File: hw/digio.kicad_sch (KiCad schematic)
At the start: 11 parts, among them U17 SN74LVC2T45DCUR

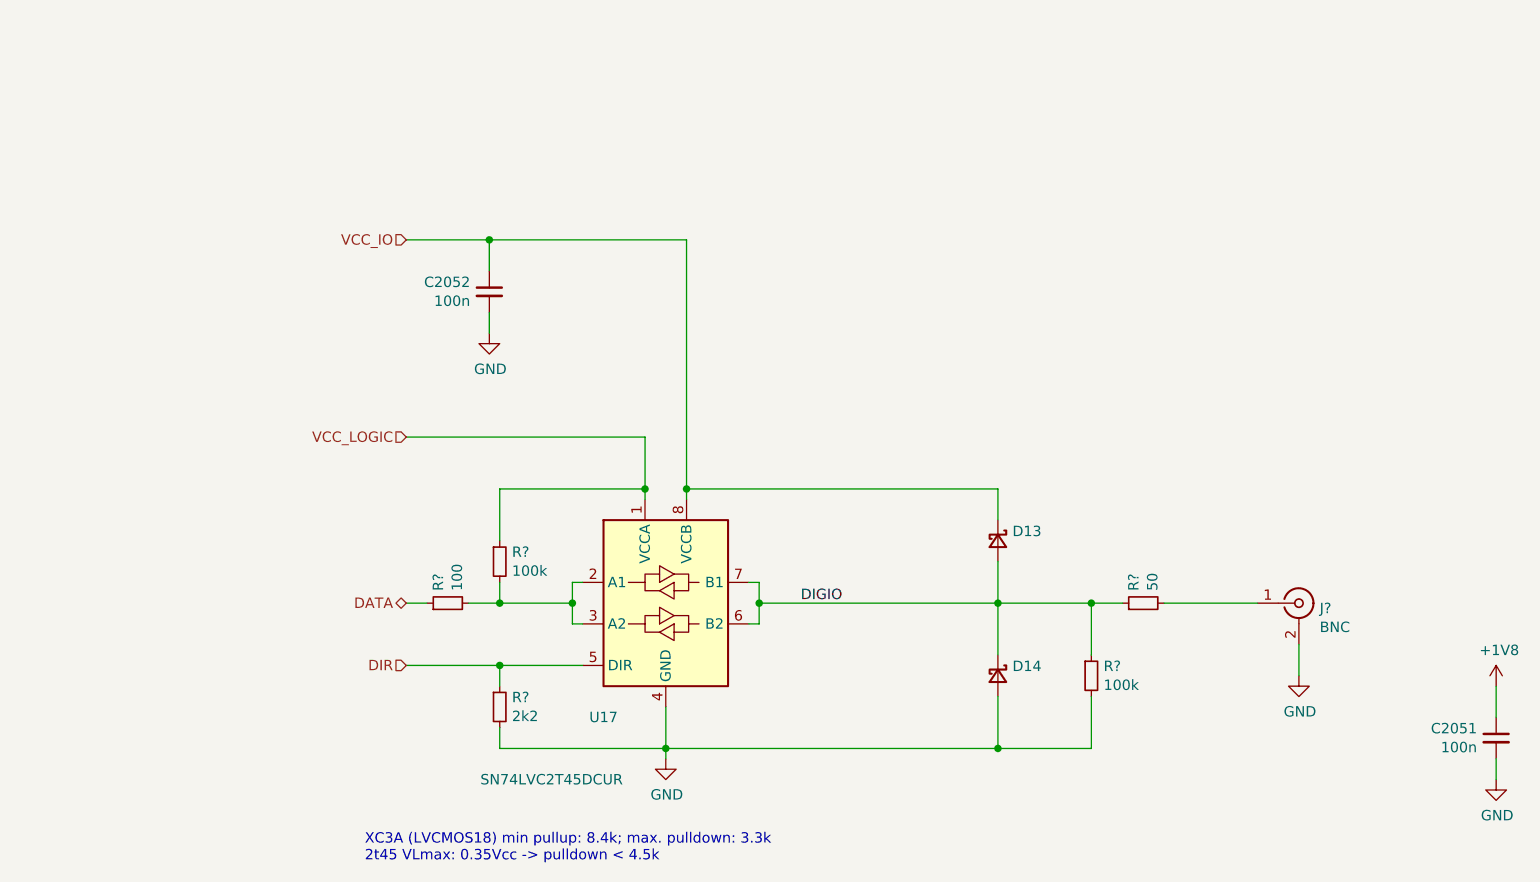
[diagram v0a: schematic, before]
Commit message: basic schematic, started layout (placing first components)
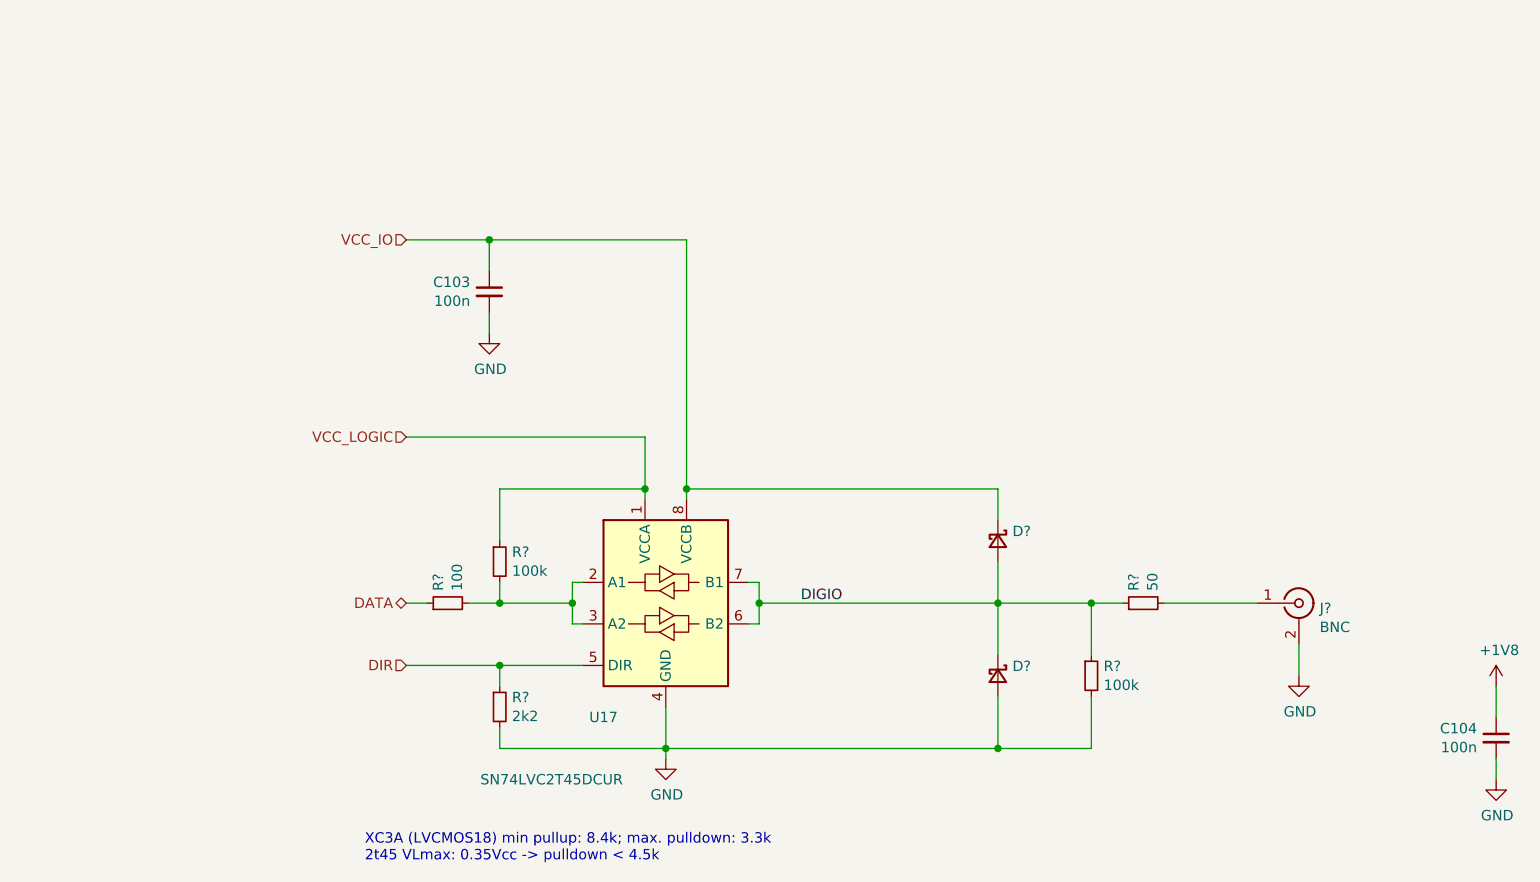
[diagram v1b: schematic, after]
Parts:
- renumbered C2052 to C103, C2051 to C104, D14 to D?, D13 to D?
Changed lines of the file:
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@@
     (effects (font (size 1.27 1.27)) (justify left bottom))
   )
-  (label "DIGIO" (at 152.4 105.41 0)
+  (label "DIGIO" (at 152.4 105.41 0) (fields_autoplaced)
     (effects (font (size 1.27 1.27)) (justify left bottom))
   )
-  (hierarchical_label "DATA" (shape bidirectional) (at 104.14 105.41 180)
+  (hierarchical_label "DATA" (shape bidirectional) (at 104.14 105.41 180) (fields_autoplaced)
     (effects (font (size 1.27 1.27)) (justify right))
   )
-  (hierarchical_label "VCC_LOGIC" (shape input) (at 104.14 85.09 180)
+  (hierarchical_label "VCC_LOGIC" (shape input) (at 104.14 85.09 180) (fields_autoplaced)
     (effects (font (size 1.27 1.27)) (justify right))
   )
-  (hierarchical_label "DIR" (shape input) (at 104.14 113.03 180)
+  (hierarchical_label "DIR" (shape input) (at 104.14 113.03 180) (fields_autoplaced)
     (effects (font (size 1.27 1.27)) (justify right))
   )
-  (hierarchical_label "VCC_IO" (shape input) (at 104.14 60.96 180)
+  (hierarchical_label "VCC_IO" (shape input) (at 104.14 60.96 180) (fields_autoplaced)
     (effects (font (size 1.27 1.27)) (justify right))
   )
@@
           (reference "J?") (unit 1)
         )
-        (path "/7c8a1f8d-8834-4c9b-aaae-1f231e9b09a1/00000000-0000-0000-0000-0000612b1274/00000000-0000-0000-0000-0000611e90a8"
-          (reference "J?") (unit 1)
-        )
         (path "/7c8a1f8d-8834-4c9b-aaae-1f231e9b09a1/00000000-0000-0000-0000-000060aabc24/00000000-0000-0000-0000-000060f79994"
           (reference "J10") (unit 1)
-        )
-        (path "/7c8a1f8d-8834-4c9b-aaae-1f231e9b09a1/00000000-0000-0000-0000-0000612b1274/00000000-0000-0000-0000-0000611783bc"
-          (reference "J?") (unit 1)
         )
         (path "/7c8a1f8d-8834-4c9b-aaae-1f231e9b09a1/00000000-0000-0000-0000-000060b16d71"
@@
   (symbol (lib_id "Device:C_Small") (at 237.49 121.92 0) (mirror y) (unit 1)
     (in_bom yes) (on_board yes) (dnp no)
-    (property "Reference" "C2051" (at 235.1532 120.7516 0)
+    (property "Reference" "C104" (at 235.1532 120.7516 0)
       (effects (font (size 1.27 1.27)) (justify left))
     )
@@
   (symbol (lib_id "Device:C_Small") (at 114.3 67.31 0) (mirror y) (unit 1)
     (in_bom yes) (on_board yes) (dnp no)
-    (property "Reference" "C2052" (at 111.9632 66.1416 0)
+    (property "Reference" "C103" (at 111.9632 66.1416 0)
       (effects (font (size 1.27 1.27)) (justify left))
     )
@@
   (symbol (lib_id "Device:D_Schottky_Small") (at 176.53 114.3 270) (unit 1)
     (in_bom yes) (on_board yes) (dnp no)
-    (property "Reference" "D14" (at 178.308 113.1316 90)
+    (property "Reference" "D?" (at 178.308 113.1316 90)
       (effects (font (size 1.27 1.27)) (justify left))
     )
@@
   (symbol (lib_id "Device:D_Schottky_Small") (at 176.53 97.79 270) (unit 1)
     (in_bom yes) (on_board yes) (dnp no)
-    (property "Reference" "D13" (at 178.308 96.6216 90)
-      (effects (font (size 1.27 1.27)) (justify left))
-    )
+    (property "Reference" "D?" (at 178.308 96.6216 90)
+      (effects (font (size 1.27 1.27)) (justify left))
+    )

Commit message: WIP (layout)
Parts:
- removed C103, C104: 100n, Capacitor_SMD:C_0402_1005Metric, symbol Device:C_Small
- removed D? (x2): NSR0170HT1G, Diode_SMD:D_SOD-323, symbol Device:D_Schottky_Small
- removed J?: BNC, proj_footprints:BNC_Molex_0731713150, symbol Connector:Conn_Coaxial
- removed R?: 2k2, Resistor_SMD:R_0603_1608Metric, symbol Device:R_Small
- removed R? (x2): 100k, Resistor_SMD:R_0603_1608Metric, symbol Device:R_Small
- removed R?: 50, Resistor_SMD:R_0603_1608Metric, symbol Device:R_Small
- removed R?: 100, Resistor_SMD:R_0603_1608Metric, symbol Device:R_Small
- added C2051, C2052: 100n, Capacitor_SMD:C_0402_1005Metric, symbol Device:C_Small
- added D13, D14: NSR0170HT1G, Diode_SMD:D_SOD-323, symbol Device:D_Schottky_Small
- added J?: BNC, proj_footprints:BNC_Molex_0731713150, symbol Connector:Conn_Coaxial
- added R?: 100, Resistor_SMD:R_0603_1608Metric, symbol Device:R_Small
- added R?: 50, Resistor_SMD:R_0603_1608Metric, symbol Device:R_Small
- added R?: 2k2, Resistor_SMD:R_0603_1608Metric, symbol Device:R_Small
- added R? (x2): 100k, Resistor_SMD:R_0603_1608Metric, symbol Device:R_Small
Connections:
- net +1V8: now also C2051.1
- net DATA: now also R?.1
- net DIGIO: now also D13.2 (A), D14.1 (K), R?.1, R?.1
- net DIR: now also R?.1
- net GND: now also C2051.2, C2052.2, D14.2 (A), J?.2 (Ext), R?.2, R?.2
- net VCC_IO: now also C2052.1, D13.1 (K)
- net VCC_LOGIC: now also R?.1
- net at U17.2 (A1), U17.3 (A2): now also R?.2, R?.2
- new net: J?.1 (In), R?.2
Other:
- note added: "(LVCMOS18) min pullup: 8.4k; max. pulldown: 3.3k 2t45 VLmax: 0.35Vcc -> pulldown < 4.5k"
- note removed: "XC3A (LVCMOS18) min pullup: 8.4k; max. pulldown: 3.3k 2t45 VLmax: 0.35Vcc -> pulldown < 4.5k"

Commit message: WIP - a lot already laid out.
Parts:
- removed C2051: 100n, Capacitor_SMD:C_0402_1005Metric, symbol Device:C_Small
- added C2052: 100n, Capacitor_SMD:C_0603_1608Metric, symbol Device:C_Small
- C2052: footprint Capacitor_SMD:C_0402_1005Metric -> Capacitor_SMD:C_0603_1608Metric
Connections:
- net GND: now also C2052.2
- net VCC_LOGIC: now also C2052.1
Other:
- moved on the sheet: C2052

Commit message: consolidated components to simplify BOM
(nothing actually changed but the symbols representing identical
components are now identical -> no more multiple BOM entries for
the same type of component).
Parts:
- C2052: Manufacturer (none) -> Samsung; Part (none) -> CL10B104KB8NFN
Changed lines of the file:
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@@
+      (effects (font (size 1.27 1.27)) hide)
+    )
+    (property "Manufacturer" "Samsung" (at 81.915 81.915 0)
+      (effects (font (size 1.27 1.27)) hide)
+    )
+    (property "Part" "CL10B104KB8NFN" (at 81.915 81.915 0)
       (effects (font (size 1.27 1.27)) hide)
     )
@@
       (effects (font (size 1.27 1.27)) hide)
     )
+    (property "Manufacturer" "Samsung" (at 81.915 57.785 0)
+      (effects (font (size 1.27 1.27)) hide)
+    )
+    (property "Part" "CL10B104KB8NFN" (at 81.915 57.785 0)
+      (effects (font (size 1.27 1.27)) hide)
+    )

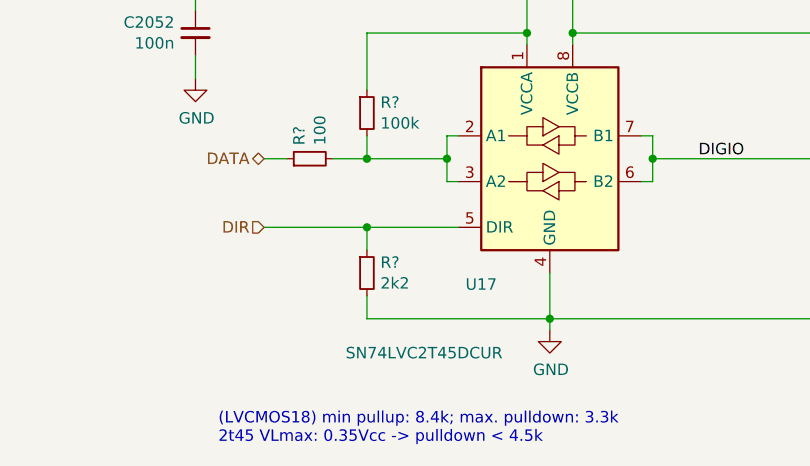
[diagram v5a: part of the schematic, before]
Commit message: Moved LEDs from +5V to 3V3. Removed LED driver FETs.
NOTE: the 3V3 connection is provisional and needs to be
reworked along with the redesign of the 5V net.

The temporary connections exist just to satisfy DRC for now.
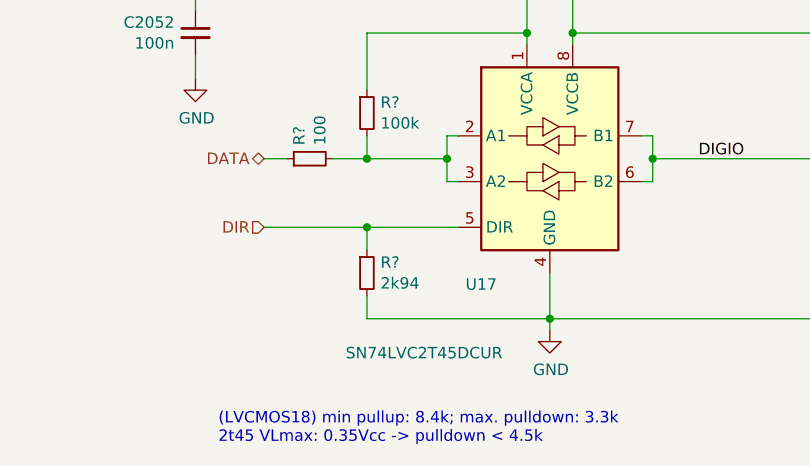
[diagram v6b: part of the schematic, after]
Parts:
- R?: value 2k2 -> 2k94
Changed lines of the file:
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@@
       (effects (font (size 1.27 1.27)) (justify left))
     )
-    (property "Value" "2k2" (at 102.4636 109.728 0)
+    (property "Value" "2k94" (at 102.4636 109.728 0)
       (effects (font (size 1.27 1.27)) (justify left))
     )

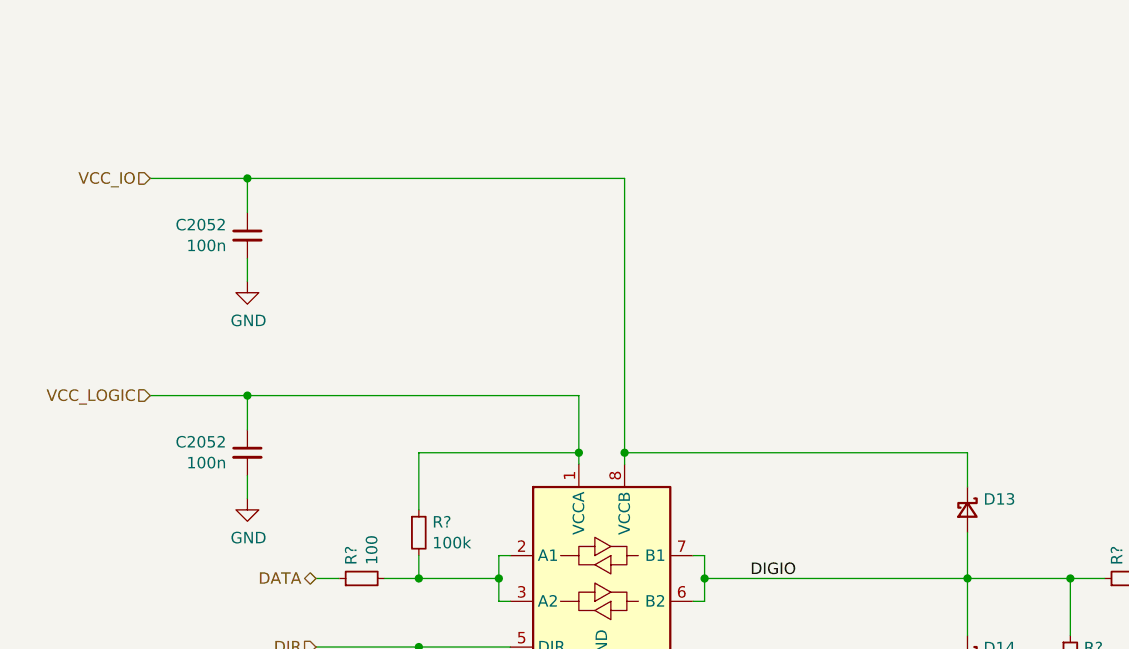
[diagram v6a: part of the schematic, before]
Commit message: added jumperable VDDIO for digital I/O, added reset generator
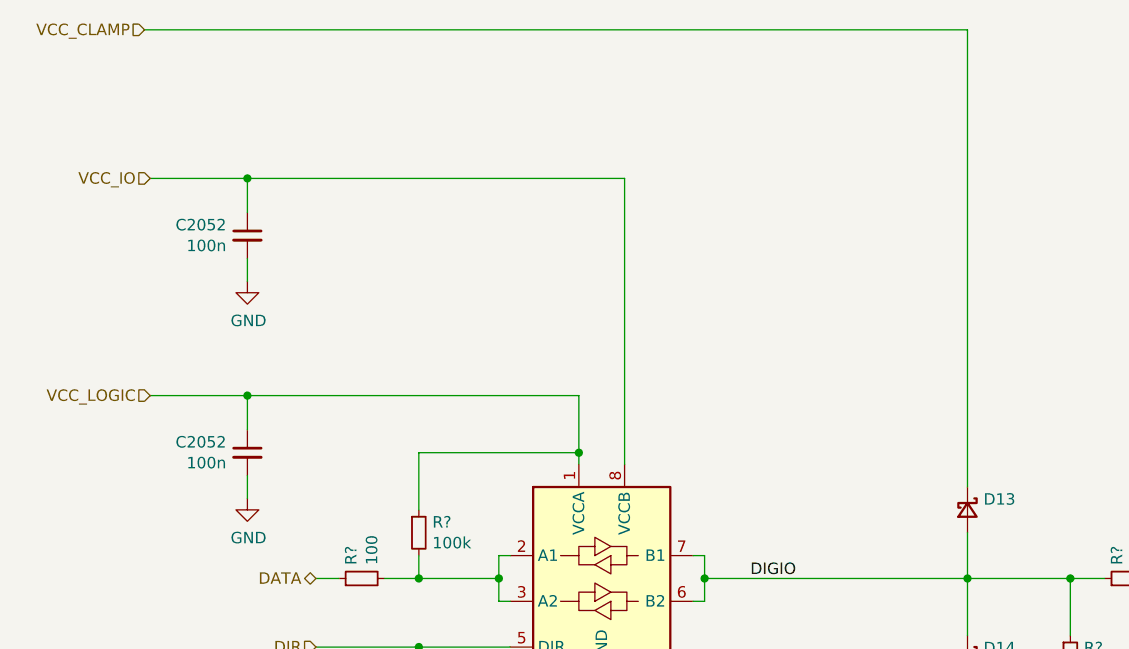
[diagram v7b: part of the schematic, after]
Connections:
- net VCC_IO: no longer D13.1 (K)
- new net VCC_CLAMP: D13.1 (K)
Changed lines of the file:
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@@
   (junction (at 100.965 95.885) (diameter 0) (color 0 0 0 0)
-  )
-  (junction (at 123.825 81.915) (diameter 0) (color 0 0 0 0)
   )
   (junction (at 132.715 95.885) (diameter 0) (color 0 0 0 0)
@@
     (stroke (width 0) (type default))
   )
-  (wire (pts (xy 123.825 81.915) (xy 123.825 83.185))
+  (wire (pts (xy 123.825 51.435) (xy 123.825 83.185))
     (stroke (width 0) (type default))
   )
@@
     (stroke (width 0) (type default))
   )
-  (wire (pts (xy 161.925 81.915) (xy 161.925 85.725))
+  (wire (pts (xy 161.925 34.925) (xy 161.925 85.725))
     (stroke (width 0) (type default))
   )
@@
     (stroke (width 0) (type default))
   )
-  (wire (pts (xy 123.825 81.915) (xy 161.925 81.915))
-    (stroke (width 0) (type default))
-  )
   (wire (pts (xy 109.855 93.345) (xy 111.125 93.345))
     (stroke (width 0) (type default))
@@
     (stroke (width 0) (type default))
   )
-  (wire (pts (xy 123.825 51.435) (xy 123.825 81.915))
+  (wire (pts (xy 161.925 34.925) (xy 70.485 34.925))
     (stroke (width 0) (type default))
   )
@@
     (effects (font (size 1.27 1.27)) (justify right))
   )
+  (hierarchical_label "VCC_CLAMP" (shape input) (at 70.485 34.925 180) (fields_autoplaced)
+    (effects (font (size 1.27 1.27)) (justify right))
+  )

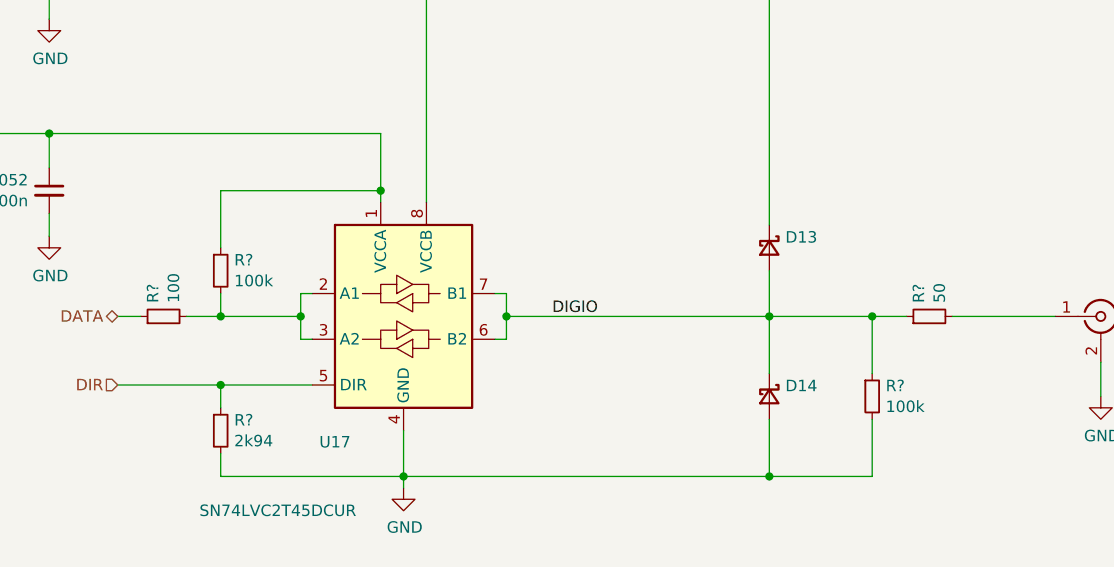
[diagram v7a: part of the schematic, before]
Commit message: Modified DAC resistors/range; connect + pull-up ADC SHDN
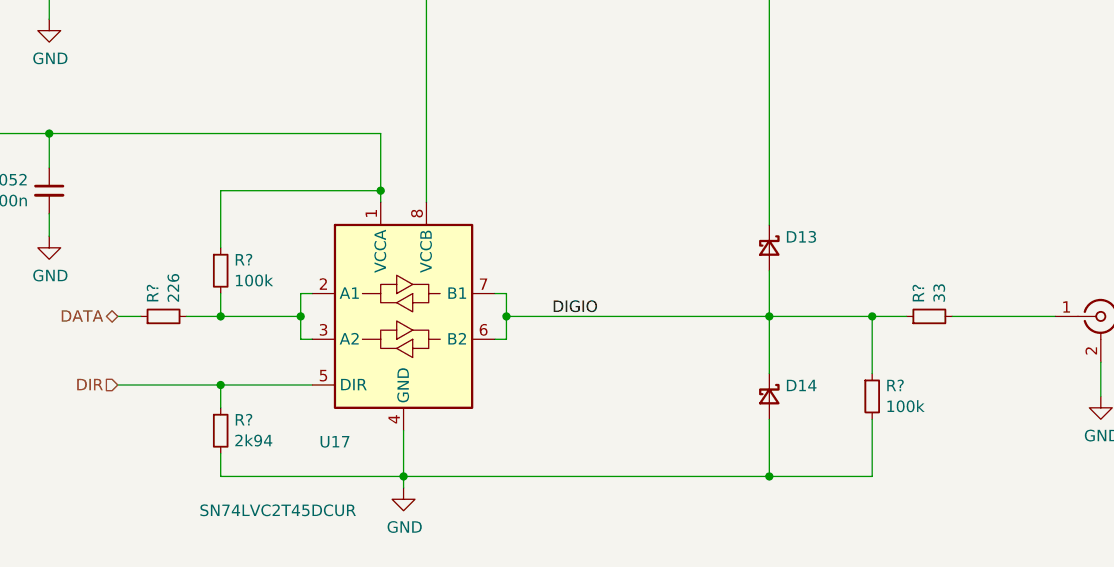
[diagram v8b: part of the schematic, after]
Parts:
- R?: value 100 -> 226
- R?: value 50 -> 33
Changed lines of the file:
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@@
       (effects (font (size 1.27 1.27)) (justify left))
     )
-    (property "Value" "100" (at 95.758 94.3864 0)
+    (property "Value" "226" (at 95.758 94.3864 0)
       (effects (font (size 1.27 1.27)) (justify left))
     )
@@
       (effects (font (size 1.27 1.27)) (justify left))
     )
-    (property "Value" "50" (at 180.848 94.3864 0)
+    (property "Value" "33" (at 180.848 94.3864 0)
       (effects (font (size 1.27 1.27)) (justify left))
     )
